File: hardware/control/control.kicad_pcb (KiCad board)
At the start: 2 copper layers, 180 x 70 mm, 46 parts, among them IC1 TMUX4053DYYR, J0 43045-0412, J1 Conn_01x02_Pin, J11 Conn_01x04_Pin, J12 Camera Isolated triggers (ope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, J2 Conn_01x02_Pin, J3 Conn_01x02_Pin, J4 Conn_01x02_Pin, J5 Conn_01x05_Pin, J6 Conn_01x04_Pin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

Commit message: external spi temp chip
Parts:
- removed C3: 0.1uF, Capacitor_THT:C_Disc_D5.0mm_W2.5mm_P2.50mm
- removed U3: MAX6675ISA_, MAX6675ISA_:SOIC127P600X175-8N
- added R11: 10k, Resistor_THT:R_Axial_DIN0207_L6.3mm_D2.5mm_P10.16mm_Horizontal, F.Cu at (213.0, 54.0)
- J7: value Screw_Terminal_01x02 -> Conn_01x08_Pin; footprint TerminalBlock_Phoenix:TerminalBlock_Phoenix_MKDS-1,5-2_1x02_P5.00mm_Horizontal -> Connector_Molex:Molex_PicoBlade_53047-0810_1x08_P1.25mm_Vertical
- moved J7 59.8 mm to (222.5, 55.2), turned to -90 degrees
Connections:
- A1 pad 14: unconnected-(A1-MOSI-Pad14) -> Net-(A1-MOSI)
- J7 pad 1: GND -> Net-(A1-SCK)
- J7 pad 2: Net-(J7-Pin_2) -> GND
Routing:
- net Net-(J7-Pin_2): track 78.6 -> 0.00 mm
- net Net-(A1-MOSI): track 0.00 -> 15.6 mm
- net Net-(A1-SCK): track 24.4 -> 37.0 mm
- net GND: track 30.8 -> 25.7 mm
- net Net-(A1-D10): track 17.8 -> 22.4 mm
- net Net-(A1-MISO): track 8.14 -> 11.8 mm
- net +5V: track 145.9 -> 145.1 mm

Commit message: added alert pullup
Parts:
- added R12: 10k, Resistor_THT:R_Axial_DIN0207_L6.3mm_D2.5mm_P10.16mm_Horizontal, F.Cu at (228.0, 62.9)
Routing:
- net unconnected-(J7-Pin_3-Pad3): track 0.00 -> 7.67 mm
- net +5V: track 145.1 -> 149.9 mm

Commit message: rework pcb layout
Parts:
- moved J6 22.2 mm to (252.5, 96.0)
- moved J5 22.2 mm to (252.5, 82.3)
- moved H2 20.0 mm to (255.0, 55.0)
- moved H3 20.0 mm to (255.0, 115.0)
- moved R11 19.6 mm to (232.5, 56.1)
- moved J7 19.4 mm to (240.5, 62.5), turned to 0 degrees
- moved A1 19.4 mm to (227.2, 99.2)
- moved J12 19.4 mm to (222.0, 115.0)
- moved J8 19.4 mm to (213.2, 115.1)
- moved R10 19.4 mm to (207.1, 81.6)
- moved R3 19.4 mm to (193.4, 71.5)
- moved R5 19.4 mm to (200.6, 97.4)
- moved TP1 19.4 mm to (189.4, 85.7)
- moved TP4 19.4 mm to (207.6, 67.0)
- moved C1 19.4 mm to (190.8, 94.2)
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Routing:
- net +12V: track 123.2 -> 153.3 mm
- net +5V: track 149.9 -> 174.6 mm
- net Net-(IC1-D3): track 100.3 -> 121.1 mm
- net Net-(IC1-D1): track 64.6 -> 85.2 mm
- net Net-(IC1-D2): track 28.9 -> 49.0 mm
- net +48V: track 175.8 -> 186.6 mm
- net Net-(A1-MOSI): track 15.6 -> 24.2 mm
- net Net-(A1-D10): track 22.4 -> 30.9 mm
- net GND: track 25.7 -> 20.2 mm
- net Net-(A1-D4): track 29.7 -> 35.1 mm
- net Net-(J4-Pin_2): track 24.0 -> 20.0 mm
- net Net-(J4-Pin_1): track 24.2 -> 20.2 mm
- net Net-(J3-Pin_2): track 24.0 -> 20.0 mm
- net Net-(J3-Pin_1): track 24.2 -> 20.2 mm
- net Net-(J2-Pin_2): track 24.0 -> 20.0 mm
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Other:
- board size 180 x 70 mm -> 200 x 70 mm
- board text removed: "K thermocouple"

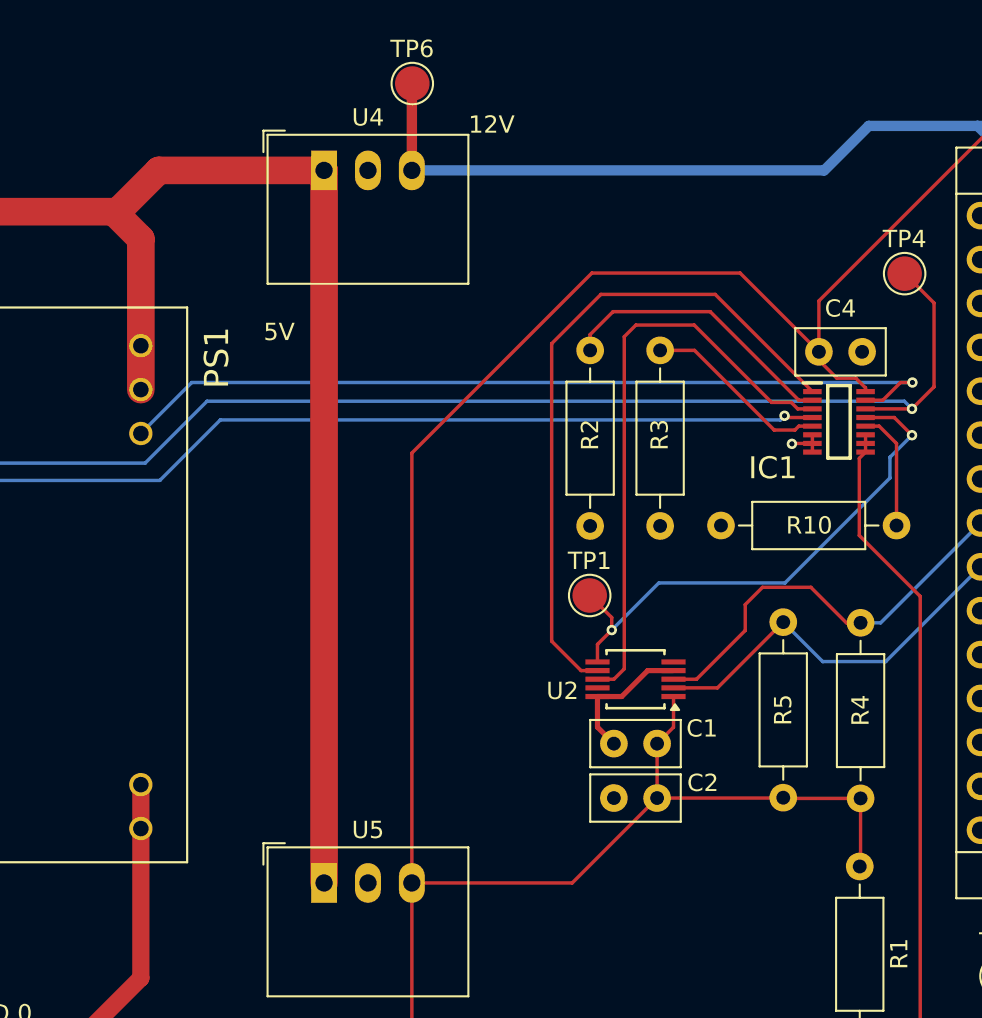
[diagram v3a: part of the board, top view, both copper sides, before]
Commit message: removing 90deg turns
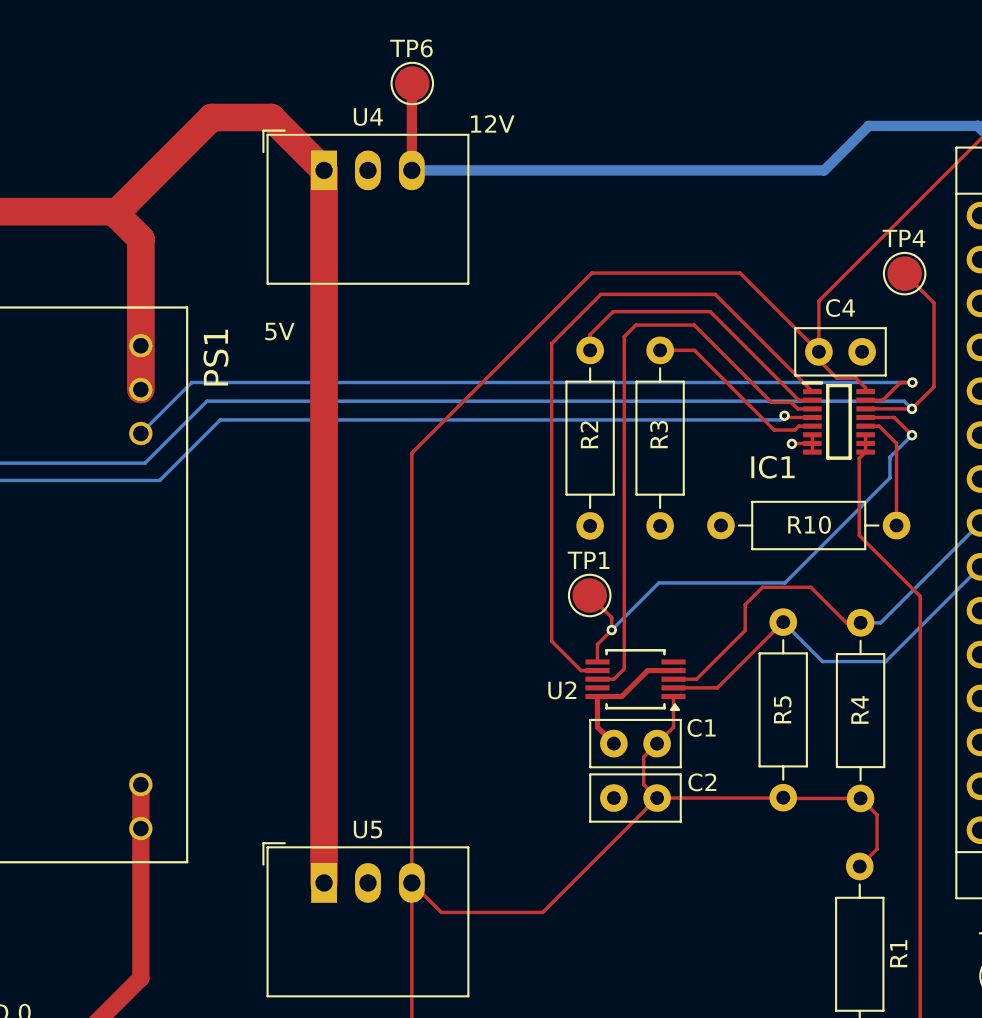
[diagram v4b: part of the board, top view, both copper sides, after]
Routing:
- net +5V: track 174.6 -> 177.5 mm
- net +48V: track 186.6 -> 189.1 mm
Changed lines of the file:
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@@
+	)
+	(segment
+		(start 162.05 63.45)
+		(end 167.5 58)
+		(width 1.6)
+		(layer "F.Cu")
+		(net "+48V")
 	)
 	(segment
@@
 	)
 	(segment
-		(start 164.44 61.06)
-		(end 174.0025 61.06)
-		(width 1.6)
-		(layer "F.Cu")
-		(net "+48V")
-	)
-	(segment
 		(start 163.4 65.025)
 		(end 163.4 73.745)
@@
 	)
 	(segment
+		(start 167.5 58)
+		(end 170.9425 58)
+		(width 1.6)
+		(layer "F.Cu")
+		(net "+48V")
+	)
+	(segment
 		(start 134.81 63.45)
 		(end 136.900832 65.540832)
@@
 	)
 	(segment
-		(start 162.05 63.45)
-		(end 164.44 61.06)
-		(width 1.6)
-		(layer "F.Cu")
-		(net "+48V")
-	)
-	(segment
 		(start 161.825 63.45)
 		(end 162.05 63.45)
+		(width 1.6)
+		(layer "F.Cu")
+		(net "+48V")
+	)
+	(segment
+		(start 170.9425 58)
+		(end 174.0025 61.06)
 		(width 1.6)
 		(layer "F.Cu")
@@
 	)
 	(segment
+		(start 206 100.34)
+		(end 205 101.34)
+		(width 0.2)
+		(layer "F.Cu")
+		(net "+5V")
+	)
+	(segment
 		(start 218 53.25)
 		(end 246.33 53.25)
@@
 	)
 	(segment
-		(start 205.048745 101.291255)
-		(end 205 101.34)
-		(width 0.2)
-		(layer "F.Cu")
-		(net "+5V")
-	)
-	(segment
-		(start 205.048745 97.399592)
-		(end 205.048745 101.291255)
-		(width 0.2)
-		(layer "F.Cu")
-		(net "+5V")
-	)
-	(segment
 		(start 205.008745 97.359592)
 		(end 205.048745 97.399592)
@@
 	)
 	(segment
-		(start 188.360837 102.2925)
-		(end 193.273745 97.379592)
+		(start 192.5 96.605847)
+		(end 192.5 95.003337)
 		(width 0.2)
 		(layer "F.Cu")
@@
 	)
 	(segment
+		(start 205.048745 97.399592)
+		(end 206 98.350847)
+		(width 0.2)
+		(layer "F.Cu")
+		(net "+5V")
+	)
+	(segment
 		(start 246.33 53.25)
 		(end 249.08 56)
@@
 	)
 	(segment
+		(start 186.653337 104)
+		(end 193.273745 97.379592)
+		(width 0.2)
+		(layer "F.Cu")
+		(net "+5V")
+	)
+	(segment
 		(start 194.223745 93.279592)
 		(end 193.273745 94.229592)
@@
 	)
 	(segment
+		(start 193.273745 97.379592)
+		(end 192.5 96.605847)
+		(width 0.2)
+		(layer "F.Cu")
+		(net "+5V")
+	)
+	(segment
 		(start 179.0825 114.4175)
 		(end 179 114.5)
@@
 	)
 	(segment
-		(start 179.0825 102.2925)
-		(end 188.360837 102.2925)
-		(width 0.2)
-		(layer "F.Cu")
-		(net "+5V")
-	)
-	(segment
 		(start 202.636745 71.559592)
 		(end 202.636745 68.613255)
@@
 	)
 	(segment
+		(start 206 98.350847)
+		(end 206 100.34)
+		(width 0.2)
+		(layer "F.Cu")
+		(net "+5V")
+	)
+	(segment
+		(start 180.79 104)
+		(end 186.653337 104)
+		(width 0.2)
+		(layer "F.Cu")
+		(net "+5V")
+	)
+	(segment
 		(start 200.553745 97.379592)
 		(end 200.573745 97.359592)
@@
 	)
 	(segment
+		(start 192.5 95.003337)
+		(end 193.273745 94.229592)
+		(width 0.2)
+		(layer "F.Cu")
+		(net "+5V")
+	)
+	(segment
 		(start 205.048745 97.399592)
 		(end 200.613745 97.399592)
@@
 	)
 	(segment
-		(start 193.273745 97.379592)
-		(end 193.273745 94.229592)
-		(width 0.2)
-		(layer "F.Cu")
+		(start 179.0825 102.2925)
+		(end 180.79 104)
+		(width 0.2)
+		(layer "F.Cu")
